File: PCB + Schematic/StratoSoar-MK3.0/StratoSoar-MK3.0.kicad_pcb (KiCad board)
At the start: 2 copper layers, 115 parts, among them J10 SWD, J11 Signal, J12 Rudder, J15 Parachute, J16 Elevator, J18 USB-C, J3 USB-C, J4 J Link, J8 Button, Q1 DMN1019USN-13, Q2 2N3906, Q3 DMN1019USN-13, Q4 DMN1019USN-13, Q5 2N3906, Q6 2N3906, SW1 RESET, SW2 PWR_SW, SW4 RESET, SW5 EEPROM, U1 AMS1117-3.3, U10 ATXK-H11-E-32.768, U11 DSK321STD, U2 ATSAMD21G18A-A, U3 MCP1700x-330xxTT, U4 ATSAMD21G18A-A, U5 BME280, U6 AT24C512C-SSHD-T, U7 ATXK-H11-E-32.768, U8 MAX-M10S, U9 MPU-9250, Y1 32.768 kHz, Y2 32.768kHz

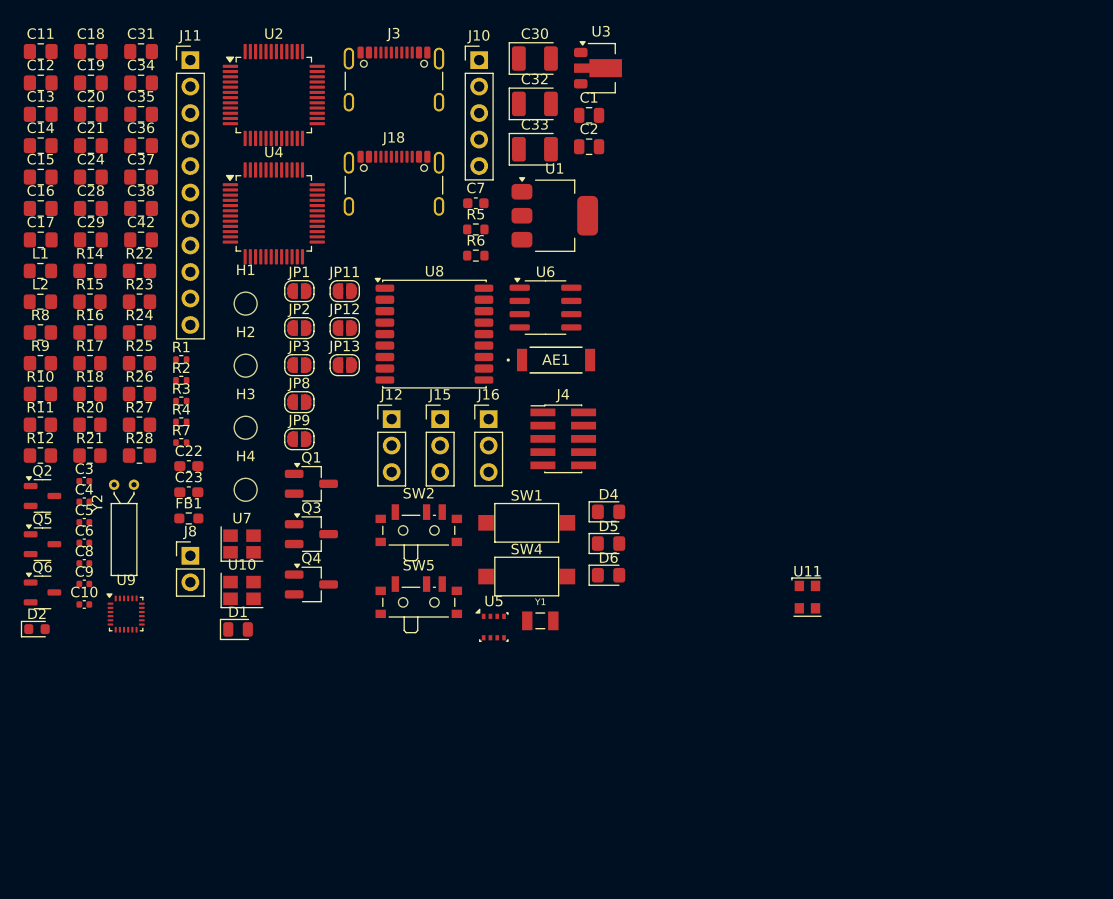
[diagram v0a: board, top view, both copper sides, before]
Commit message: Finished schematic, started PCB
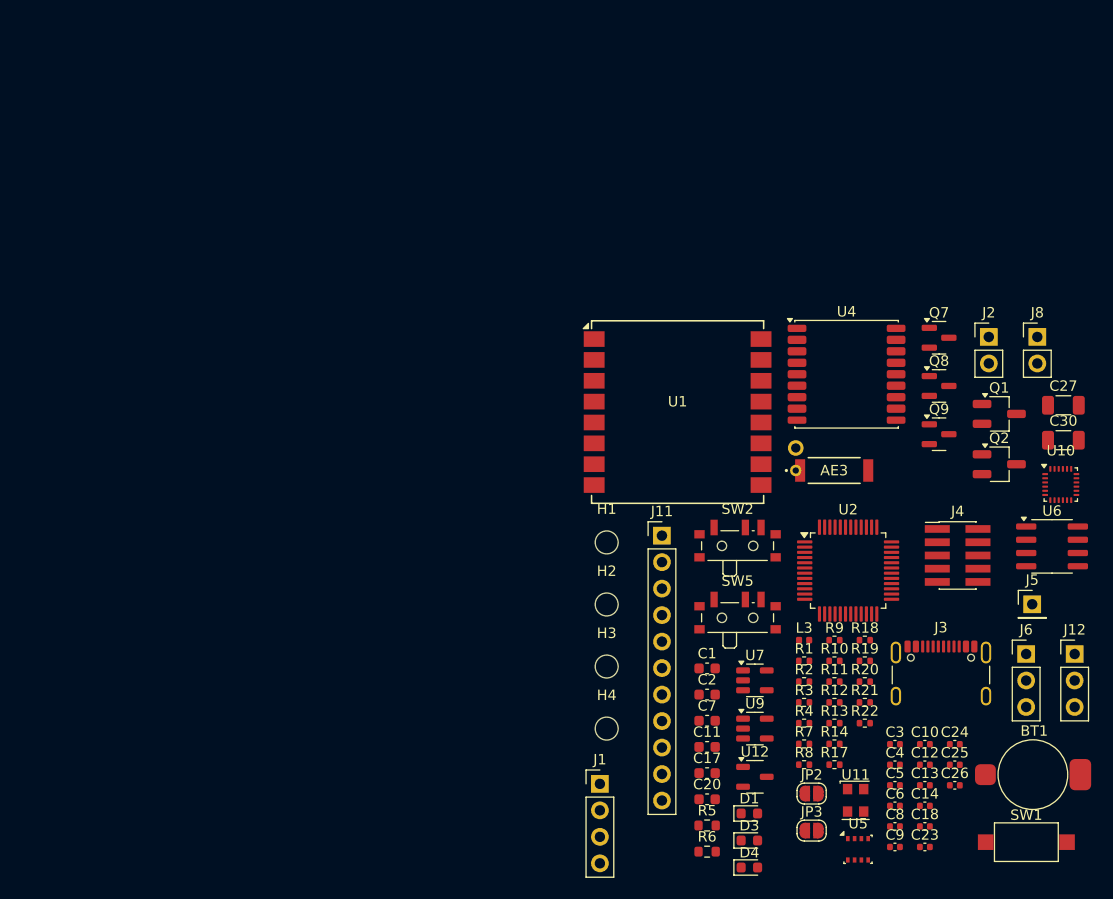
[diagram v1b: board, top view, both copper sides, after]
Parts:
- removed AE1: 1575AT43A0040001E, 1575AT43A0040E:ANT_1575AT_JOT-L
- removed C15, C16, C19, C34, C36, C37, C38, C42: 100nF, Capacitor_SMD:C_0805_2012Metric_Pad1.18x1.45mm_HandSolder
- removed C21: 1 uF, Capacitor_SMD:C_0805_2012Metric_Pad1.18x1.45mm_HandSolder
- removed C22: 100nF, Capacitor_SMD:C_0603_1608Metric_Pad1.08x0.95mm_HandSolder
- removed C28, C29: 22pF, Capacitor_SMD:C_0805_2012Metric_Pad1.18x1.45mm_HandSolder
- removed C31: 100pF, Capacitor_SMD:C_0805_2012Metric_Pad1.18x1.45mm_HandSolder
- removed C32, C33: 47uF, Capacitor_Tantalum_SMD:CP_EIA-3528-21_Kemet-B
- removed C35: 10nF, Capacitor_SMD:C_0805_2012Metric_Pad1.18x1.45mm_HandSolder
- removed D2: LED, LED_SMD:LED_0603_1608Metric
- removed D5: ERR_LED, LED_SMD:LED_0805_2012Metric_Pad1.15x1.40mm_HandSolder
- removed D6: LED, LED_SMD:LED_0805_2012Metric_Pad1.15x1.40mm_HandSolder
- removed FB1: BLM18AG121SN1D, Resistor_SMD:R_0603_1608Metric_Pad0.98x0.95mm_HandSolder
- removed J10: SWD, Connector_PinHeader_2.54mm:PinHeader_1x05_P2.54mm_Vertical
- removed J15: Parachute, Connector_PinHeader_2.54mm:PinHeader_1x03_P2.54mm_Vertical
- removed J16: Elevator, Connector_PinHeader_2.54mm:PinHeader_1x03_P2.54mm_Vertical
- removed J18: USB-C, Connector_USB:USB_C_Receptacle_GCT_USB4105-xx-A_16P_TopMnt_Horizontal
- removed JP1: PWR_EN, Jumper:SolderJumper-2_P1.3mm_Open_RoundedPad1.0x1.5mm
- removed JP11: LED_EN, Jumper:SolderJumper-2_P1.3mm_Open_RoundedPad1.0x1.5mm
- removed JP12: ERR_LED_EN, Jumper:SolderJumper-2_P1.3mm_Open_RoundedPad1.0x1.5mm
- removed JP13: PPS_EN, Jumper:SolderJumper-2_P1.3mm_Open_RoundedPad1.0x1.5mm
- removed JP8, JP9: XO_EN, Jumper:SolderJumper-2_P1.3mm_Open_RoundedPad1.0x1.5mm
- removed L1: 10uH, Inductor_SMD:L_0805_2012Metric_Pad1.15x1.40mm_HandSolder
- removed L2: 33nH, Inductor_SMD:L_0805_2012Metric_Pad1.15x1.40mm_HandSolder
- removed Q3, Q4: DMN1019USN-13, Package_TO_SOT_SMD:SC-59_Handsoldering
- removed Q5, Q6: 2N3906, Package_TO_SOT_SMD:SOT-23-3
- removed R15, R16: 1.8K, Resistor_SMD:R_0805_2012Metric_Pad1.20x1.40mm_HandSolder
- removed R23: 10, Resistor_SMD:R_0805_2012Metric_Pad1.20x1.40mm_HandSolder
- removed R24, R25: 5.1K, Resistor_SMD:R_0805_2012Metric_Pad1.20x1.40mm_HandSolder
- removed R26, R27, R28: 1K, Resistor_SMD:R_0805_2012Metric_Pad1.20x1.40mm_HandSolder
- removed SW4: RESET, Button_Switch_SMD:SW_SPST_CK_RS282G05A3
- removed U3: MCP1700x-330xxTT, Package_TO_SOT_SMD:SOT-89-3
- removed U8: MAX-M10S, RF_GPS:ublox_MAX
- removed Y1: 32.768 kHz, CM7V-T1A-32.768K-12.5PF-20PPM-TA-QA:XTAL_CM7V-T1A-32.768K-12.5PF-20PPM-TA-QA
- removed Y2: 32.768kHz, Crystal:Crystal_C26-LF_D2.1mm_L6.5mm_Horizontal
- added AE3: 1575AT43A0040001E, 1575AT43A0040E:ANT_1575AT_JOT-L, F.Cu at (142.3, 80.7)
- added BT1: MS621R, Battery:MS621R, F.Cu at (156.7, 109.9)
- added C25: 100 pF, Capacitor_SMD:C_0402_1005Metric, F.Cu at (153.8, 108.9)
- added C26: 100 nF, Capacitor_SMD:C_0402_1005Metric, F.Cu at (153.8, 110.9)
- added C27: 47 uF, Capacitor_SMD:C_1206_3216Metric, F.Cu at (164.2, 74.4)
- added D3: YELLOW, LED_SMD:LED_0603_1608Metric, F.Cu at (134.1, 116.2)
- added J1: Power, Connector_PinHeader_2.54mm:PinHeader_1x04_P2.54mm_Vertical, F.Cu at (119.8, 110.7)
- added J2: Battery, Connector_PinHeader_2.54mm:PinHeader_1x02_P2.54mm_Vertical, F.Cu at (157.1, 67.9)
- added J5: Antenna, Connector_PinHeader_2.54mm:PinHeader_1x01_P2.54mm_Vertical, F.Cu at (161.3, 93.5)
- added J6: Rudder, Connector_PinHeader_2.54mm:PinHeader_1x03_P2.54mm_Vertical, F.Cu at (160.7, 98.3)
- added L3: 33 nH, Inductor_SMD:L_0402_1005Metric, F.Cu at (139.4, 97.0)
- added Q7: BSS138, Package_TO_SOT_SMD:SOT-23, F.Cu at (152.3, 68.0)
- added Q8: BSS138, Package_TO_SOT_SMD:SOT-23, F.Cu at (152.3, 72.6)
- added Q9: BSS138, Package_TO_SOT_SMD:SOT-23, F.Cu at (152.3, 77.2)
- added R13: 10 K, Resistor_SMD:R_0402_1005Metric, F.Cu at (142.3, 104.9)
- added R19: 10 K, Resistor_SMD:R_0402_1005Metric, F.Cu at (145.2, 99.0)
- added U12: XC6206P332MR-G, Package_TO_SOT_SMD:SOT-23-3, F.Cu at (134.7, 110.1)
- C1: footprint Capacitor_SMD:C_0805_2012Metric -> Capacitor_SMD:C_0603_1608Metric
- C10, C9: value 22 pF -> 100 nF
- C11: value 10uF -> 1 uF; footprint Capacitor_SMD:C_0805_2012Metric_Pad1.18x1.45mm_HandSolder -> Capacitor_SMD:C_0603_1608Metric
- C12: value 100pF -> 1 uF; footprint Capacitor_SMD:C_0805_2012Metric_Pad1.18x1.45mm_HandSolder -> Capacitor_SMD:C_0402_1005Metric
- C13: value 100nF -> 1 uF; footprint Capacitor_SMD:C_0805_2012Metric_Pad1.18x1.45mm_HandSolder -> Capacitor_SMD:C_0402_1005Metric
- C14: value 100nF -> 100 nF; footprint Capacitor_SMD:C_0805_2012Metric_Pad1.18x1.45mm_HandSolder -> Capacitor_SMD:C_0402_1005Metric
- C17: value 10uF -> 100 nF; footprint Capacitor_SMD:C_0805_2012Metric_Pad1.18x1.45mm_HandSolder -> Capacitor_SMD:C_0603_1608Metric
- C18: value 1uF -> 100 nF; footprint Capacitor_SMD:C_0805_2012Metric_Pad1.18x1.45mm_HandSolder -> Capacitor_SMD:C_0402_1005Metric
- C2: value 10 uF -> 100 nF; footprint Capacitor_SMD:C_0805_2012Metric -> Capacitor_SMD:C_0603_1608Metric
- C20: footprint Capacitor_SMD:C_0805_2012Metric_Pad1.18x1.45mm_HandSolder -> Capacitor_SMD:C_0603_1608Metric
- C23: value 1uF -> 1 uF; footprint Capacitor_SMD:C_0603_1608Metric_Pad1.08x0.95mm_HandSolder -> Capacitor_SMD:C_0402_1005Metric
- C24: footprint Capacitor_SMD:C_0805_2012Metric_Pad1.18x1.45mm_HandSolder -> Capacitor_SMD:C_0402_1005Metric
- C30: value 47uF -> 47 uF; footprint Capacitor_Tantalum_SMD:CP_EIA-3528-21_Kemet-B -> Capacitor_SMD:C_1206_3216Metric
- D1: value PWR_LED -> PWR_RED; footprint LED_SMD:LED_0805_2012Metric -> LED_SMD:LED_0603_1608Metric
- D4: value LED -> YELLOW; footprint LED_SMD:LED_0805_2012Metric_Pad1.15x1.40mm_HandSolder -> LED_SMD:LED_0603_1608Metric
- Q2: value 2N3906 -> DMN1019USN-13; footprint Package_TO_SOT_SMD:SOT-23-3 -> Package_TO_SOT_SMD:SC-59_Handsoldering
- R10: value 220 -> 1 K; footprint Resistor_SMD:R_0805_2012Metric_Pad1.20x1.40mm_HandSolder -> Resistor_SMD:R_0402_1005Metric
- R11, R12, R17, R18, R20: value 10K -> 10 K; footprint Resistor_SMD:R_0805_2012Metric_Pad1.20x1.40mm_HandSolder -> Resistor_SMD:R_0402_1005Metric
- R14, R8, R9: footprint Resistor_SMD:R_0805_2012Metric_Pad1.20x1.40mm_HandSolder -> Resistor_SMD:R_0402_1005Metric
- R21: value 10K -> 10; footprint Resistor_SMD:R_0805_2012Metric_Pad1.20x1.40mm_HandSolder -> Resistor_SMD:R_0402_1005Metric
- R22: value 10 -> 10 K; footprint Resistor_SMD:R_0805_2012Metric_Pad1.20x1.40mm_HandSolder -> Resistor_SMD:R_0402_1005Metric
- U1: value AMS1117-3.3 -> Ra-01; footprint Package_TO_SOT_SMD:SOT-223-3_TabPin2 -> RF_Module:Ai-Thinker-Ra-01-LoRa
- U10: value ATXK-H11-E-32.768 -> ICM-20948; footprint Crystal:Crystal_SMD_Abracon_ABM8AIG-4Pin_3.2x2.5mm -> Sensor_Motion:InvenSense_QFN-24_3x3mm_P0.4mm
- U4: value ATSAMD21G18A-A -> ATGM336H; footprint Package_QFP:TQFP-48_7x7mm_P0.5mm -> RF_GPS:ATGM336H
- U7: value ATXK-H11-E-32.768 -> AT24CS32-STUM; footprint Crystal:Crystal_SMD_Abracon_ABM8AIG-4Pin_3.2x2.5mm -> Package_TO_SOT_SMD:SOT-23-5
- U9: value MPU-9250 -> CJ6206B18M; footprint Sensor_Motion:InvenSense_QFN-24_3x3mm_P0.4mm -> Package_TO_SOT_SMD:SOT-23-5
- moved C18 109.2 mm to (151.0, 114.8)
- moved C12 107.1 mm to (151.0, 108.9)
- moved C13 106.4 mm to (151.0, 110.9)
- moved C14 105.8 mm to (151.0, 112.9)
- moved C24 99.1 mm to (153.8, 106.9)
- moved C11 92.4 mm to (130.1, 107.2)
- moved Q2 91.8 mm to (158.1, 80.1)
- moved C20 88.3 mm to (130.1, 112.2)
- moved R14 84.6 mm to (142.3, 106.9)
- moved R8 84.1 mm to (139.4, 108.9)
- moved J8 83.9 mm to (161.7, 67.9)
- moved R22 82.0 mm to (145.2, 104.9)
- moved C17 81.8 mm to (130.1, 109.7)
- moved C3 81.7 mm to (148.1, 106.9)
- moved C4 81.7 mm to (148.1, 108.9)
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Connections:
- C1 pad 1: +5V -> +3.3V
- C10 pad 1: XOUT -> Net-(U10-REGOUT)
- C11 pad 1: GND -> +3.3V
- C11 pad 2: +3.3V -> GND
- C12 pad 1: Net-(U10-OUTPUT) -> +3.3V
- C12 pad 2: XIN -> GND
- C13 pad 1: +3.3V -> +1V8
- C17 pad 1: Net-(U4-VDDANA) -> GND
- C17 pad 2: GND -> +3.3V
- C18 pad 1: Net-(U4-VDDCORE) -> +3.3V
- C2 pad 1: Net-(JP1-A) -> +3.3V
- C3 pad 1: Net-(JP1-A) -> +1V8
- C30 pad 1: +5V -> VCC
- C4 pad 1: +5V -> USB_IN
- C9 pad 1: XIN -> +1V8
- J11 pad 1: A3 -> unconnected-(J11-Pin_1-Pad1)
- J11 pad 2: A4 -> unconnected-(J11-Pin_2-Pad2)
- J11 pad 3: A5 -> unconnected-(J11-Pin_3-Pad3)
- J11 pad 8: AT_SDA -> unconnected-(J11-Pin_8-Pad8)
- J11 pad 9: AT_SCL -> unconnected-(J11-Pin_9-Pad9)
- J12 pad 2: +5V -> VCC
- J12 pad 3: rOut -> R
- J3 pad A4: +5V -> USB_IN
- J3 pad A9: +5V -> USB_IN
- J3 pad B4: +5V -> USB_IN
- J3 pad B9: +5V -> USB_IN
- J4 pad 10: RST -> RESET
- J8 pad 1: A3 -> unconnected-(J8-Pin_1-Pad1)
- JP3 pad 2: 13 -> LED
- Q2 pad 1: Net-(Q2-B) -> GND
- Q2 pad 2: rOut -> Net-(Q2-G)
- Q2 pad 3: rIn -> Net-(J6-Pin_1)
- R10 pad 1: +3.3V -> Net-(D3-A)
- R10 pad 2: RESET -> PPS
- R11 pad 1: Net-(Q2-B) -> +1V8
- R11 pad 2: rBJT -> SDA_L
- R12 pad 1: GND -> Net-(Q1-G)
- R12 pad 2: Net-(Q1-G) -> GND
- R14 pad 2: rFET -> R_FET
- R17 pad 1: Net-(Q5-B) -> +3.3V
- R17 pad 2: pBJT -> SDA
- R18 pad 1: Net-(Q6-B) -> Net-(Q2-G)
- R18 pad 2: eBJT -> GND
- R20 pad 1: GND -> +1V8
- R20 pad 2: Net-(Q3-G) -> INT_L
- R21 pad 1: GND -> Net-(Q2-G)
- R21 pad 2: Net-(Q4-G) -> L_FET
- R22 pad 1: Net-(Q3-G) -> +3.3V
- R22 pad 2: pFET -> INT
- R4 pad 1: Net-(D2-A) -> Net-(D4-A)
- R7 pad 2: RST -> RESET
- SW1 pad 2: RST -> RESET
- U1 pad 1: GND -> Net-(J5-Pin_1)
- U1 pad 2: Net-(JP1-A) -> GND
- U1 pad 3: +5V -> +3.3V
- U10 pad 1: +3.3V -> unconnected-(U10-RESV_VDDIO-Pad1)
- U10 pad 2: GND -> (no net)
- U10 pad 3: Net-(U10-OUTPUT) -> (no net)
- U10 pad 4: +3.3V -> (no net)
- U11 pad 1: unconnected-(U11-VCC-Pad1) -> +3.3V
- U11 pad 2: unconnected-(U11-GND-Pad2) -> GND
- U11 pad 3: unconnected-(U11-SIG-Pad3) -> Net-(U11-SIG)
- U11 pad 4: unconnected-(U11-VCC-Pad4) -> +3.3V
- U2 pad 2: XOUT -> unconnected-(U2-PA01-Pad2)
- U2 pad 40: RST -> RESET
- U4 pad 1: XIN -> GND
- U4 pad 10: A4 -> GND
- U4 pad 11: rBJT -> GPS
- U4 pad 12: pBJT -> GND
- U4 pad 13: pIn -> (no net)
- U4 pad 14: eIn -> unconnected-(U4-VCC_RF-Pad14)
- U4 pad 15: mcuConnRX -> (no net)
- U4 pad 16: mcuConnTX -> GPS_SDA
- U4 pad 17: +3.3V -> GPS_SCL
- U4 pad 18: GND -> (no net)
- U4 pad 2: XOUT -> TX
- U4 pad 3: ERR_LED -> RX
- U4 pad 4: unconnected-(U4-PA03-Pad4) -> PPS
- U4 pad 5: GND -> +3.3V
- U4 pad 6: Net-(U4-VDDANA) -> V_BAT
- U4 pad 7: BATT -> (no net)
- U4 pad 8: WRITE -> +3.3V
- U4 pad 9: A3 -> GPS_RST
- U7 pad 1: +3.3V -> GPS_SDA
- U7 pad 3: Net-(U7-OUTPUT) -> GPS_SDA
- U9 pad 2: (no net) -> GND
- U9 pad 3: (no net) -> +3.3V
- U9 pad 5: (no net) -> +1V8

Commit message: Basic layout
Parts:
- added C15: 100 nF, Capacitor_SMD:C_0402_1005Metric, F.Cu at (236.7, 87.1)
- C4: footprint Capacitor_SMD:C_0402_1005Metric -> Capacitor_SMD:C_0603_1608Metric
- C7: footprint Capacitor_SMD:C_0603_1608Metric -> Capacitor_SMD:C_0402_1005Metric
- JP2, JP3: moved to B.Cu
- moved U7 164.7 mm to (276.2, 16.6)
- moved C18 161.3 mm to (278.9, 16.5), turned to 90 degrees
- moved D3 158.1 mm to (259.3, 19.6), turned to 90 degrees
- moved C17 156.4 mm to (260.1, 22.9)
- moved BT1 151.1 mm to (278.1, 19.8), turned to -90 degrees
- moved R10 142.8 mm to (260.6, 19.0), turned to 90 degrees
- moved L3 140.0 mm to (261.4, 28.2), turned to 90 degrees
- moved U4 134.7 mm to (267.7, 19.5)
- moved AE3 134.7 mm to (266.5, 28.7)
- moved C8 118.0 mm to (56.0, 41.0), turned to 90 degrees
- moved C5 115.5 mm to (60.7, 35.3)
- moved C3 115.3 mm to (42.0, 152.2)
- moved C9 115.3 mm to (42.0, 162.0)
- moved Q7 115.3 mm to (46.3, 113.2)
- moved Q8 115.3 mm to (46.3, 117.8)
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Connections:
- U7 pad 1: GPS_SDA -> GPS_SCL
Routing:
- net GND: track 0.00 -> 62.2 mm, vias 0 -> 20
- net +3.3V: track 0.00 -> 28.3 mm, vias 0 -> 9
- net VCC: track 0.00 -> 8.99 mm
- net USB_IN: track 0.00 -> 8.58 mm
- net Net-(SW5-B): track 0.00 -> 5.96 mm
- net SCL: track 0.00 -> 5.27 mm
- net Net-(Q1-G): track 0.00 -> 4.99 mm
- net Net-(Q2-G): track 0.00 -> 4.99 mm
- net SDA: track 0.00 -> 3.54 mm
- net Net-(J6-Pin_1): track 0.00 -> 3.39 mm
- net Net-(J12-Pin_1): track 0.00 -> 3.05 mm
- net GPS_SCL: track 0.00 -> 2.87 mm
- net GPS_SDA: track 0.00 -> 2.75 mm
- net BATT: track 0.00 -> 2.46 mm
- net PPS: track 0.00 -> 2.42 mm
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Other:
- copper layers 2 -> 4

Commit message: IMU work
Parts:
- moved AE3 199.5 mm to (75.8, 87.0)
- moved C17 199.5 mm to (69.3, 81.2)
- moved D3 199.5 mm to (68.6, 77.9)
- moved U4 199.5 mm to (76.9, 77.8)
- moved U7 199.5 mm to (85.5, 74.9)
- moved BT1 199.5 mm to (87.4, 78.1)
- moved C18 199.5 mm to (88.1, 74.8)
- moved L3 199.5 mm to (70.6, 86.5)
- moved R10 199.5 mm to (69.8, 77.4)
- moved C2 78.4 mm to (178.9, 40.9), turned to 90 degrees
- moved C1 77.4 mm to (180.5, 40.9), turned to 90 degrees
- moved U1 71.0 mm to (191.5, 44.9)
- moved R7 69.4 mm to (164.0, 171.8), turned to 90 degrees
- moved J5 63.5 mm to (183.5, 34.0)
- moved SW1 55.0 mm to (158.5, 171.3)
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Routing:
- net +3.3V: track 28.3 -> 46.5 mm, vias 9 -> 16
- net GND: track 62.2 -> 79.3 mm, vias 20 -> 27
- net +1V8: track 0.00 -> 9.18 mm
- net Net-(J5-Pin_1): track 0.00 -> 3.91 mm
- net SCL_L: track 0.00 -> 2.05 mm
- net INT_L: track 0.00 -> 2.05 mm
- net SDA_L: track 0.00 -> 2.05 mm
- net SDA: track 3.54 -> 5.18 mm
- net SCL: track 5.27 -> 6.90 mm
- net INT: track 0.00 -> 1.63 mm
- net RESET: track 0.00 -> 1.60 mm
- net Net-(U11-SIG): track 0.00 -> 1.52 mm
- net Net-(U10-REGOUT): track 0.00 -> 1.39 mm

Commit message: Code, licensing
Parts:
- moved C12 33.4 mm to (71.5, 115.8), turned to 180 degrees
- moved U9 30.6 mm to (70.7, 113.2), turned to 90 degrees
- moved C13 28.0 mm to (70.0, 110.6), turned to 0 degrees
- moved Q7 26.0 mm to (68.8, 108.1)
- moved R19 26.0 mm to (68.0, 105.6)
- moved R13 26.0 mm to (68.0, 110.5)
- moved C9 20.8 mm to (68.3, 113.8)
- moved C10 20.8 mm to (66.9, 116.0)
- moved C3 20.8 mm to (65.0, 116.0)
- moved U10 20.8 mm to (65.7, 113.3)
- moved R11 19.6 mm to (64.6, 110.5)
- moved Q8 19.6 mm to (65.3, 108.1)
- moved R17 19.6 mm to (64.6, 105.6)
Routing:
- net +1V8: track 9.18 -> 24.6 mm
- net SCL_L: track 2.05 -> 6.20 mm
- net SDA_L: track 2.05 -> 3.49 mm
- net GND: track 79.3 -> 80.7 mm

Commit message: PCB
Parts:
- removed J11: Signal, Connector_PinHeader_2.54mm:PinHeader_1x11_P2.54mm_Vertical
- added J7: Signal, Connector_PinHeader_2.54mm:PinHeader_1x09_P2.54mm_Vertical, F.Cu at (159.8, 74.7)
- added R15: 1.8 K, Resistor_SMD:R_0603_1608Metric, F.Cu at (85.0, 73.3)
- added R16: 1.8 K, Resistor_SMD:R_0603_1608Metric, F.Cu at (85.0, 78.4)
- BT1: moved to B.Cu
- D1: value PWR_RED -> ERR_RED
- JP2: value PWR_LED_EN -> ERR_LED_EN
- moved C5 124.6 mm to (174.1, 86.7), turned to -90 degrees
- moved C7 123.2 mm to (173.9, 88.8), turned to -90 degrees
- moved C8 119.7 mm to (168.4, 82.0), turned to 0 degrees
- moved C6 116.6 mm to (170.7, 94.2), turned to 180 degrees
- moved U2 115.5 mm to (167.9, 88.3), turned to -90 degrees
- moved R6 110.0 mm to (166.2, 95.5), turned to 180 degrees
- moved R5 109.4 mm to (166.2, 97.0), turned to 180 degrees
- moved J3 105.4 mm to (190.0, 94.1), turned to 90 degrees
- moved C4 100.0 mm to (184.3, 97.3), turned to -90 degrees
- moved R2 98.5 mm to (184.2, 95.3), turned to 180 degrees
- moved R1 96.8 mm to (184.2, 92.3), turned to 180 degrees
- moved J1 79.2 mm to (192.4, 79.1)
- moved U1 69.5 mm to (167.0, 110.0), turned to -90 degrees
- moved J5 69.0 mm to (159.8, 98.8)
- moved H4 66.7 mm to (187.1, 109.6)
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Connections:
- J12 pad 3: R -> RIGHT
- J6 pad 3: L -> LEFT
- J8 pad 1: unconnected-(J8-Pin_1-Pad1) -> GND
- J8 pad 2: GND -> BTN
- JP2 pad 2: +3.3V -> ERR
- U1 pad 5: unconnected-(U1-DIO0-Pad5) -> DIO0
- U2 pad 11: D8 -> L_FET
- U2 pad 12: D9 -> RIGHT
- U2 pad 13: D4 -> BTN
- U2 pad 15: D1 -> TX
- U2 pad 16: D0 -> RX
- U2 pad 24: D5 -> DIO0
- U2 pad 25: D11 -> GPS_EN
- U2 pad 26: D13 -> LED
- U2 pad 27: D10 -> LEFT
- U2 pad 28: D12 -> ERR
- U2 pad 29: D6 -> LORA_RST
- U2 pad 3: A0 -> BATT
- U2 pad 30: D7 -> R_FET
- U4 pad 5: +3.3V -> GPS_EN
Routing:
- net VCC: track 8.99 -> 55.2 mm, vias 0 -> 1
- net +BATT: track 0.00 -> 32.6 mm, vias 0 -> 1
- net +3.3V: track 46.5 -> 73.9 mm, vias 16 -> 15
- net Net-(J5-Pin_1): track 3.91 -> 23.2 mm
- net USB_IN: track 8.58 -> 26.2 mm
- net GND: track 80.7 -> 97.6 mm, vias 27 -> 30
- net V_BAT: track 0.00 -> 8.92 mm, vias 0 -> 1
- net D2: track 0.00 -> 4.77 mm
- net GPS_SDA: track 2.75 -> 4.62 mm
- net GPS_SCL: track 2.87 -> 4.01 mm
- net ERR: track 0.00 -> 0.11 mm, vias 0 -> 1
- added copper zone on In2.Cu, net +3.3V
- added copper zone on In1.Cu, net GND
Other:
- board outline added: 253.4 x 174.4 mm

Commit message: Finished all connections on PCB
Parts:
- removed Q9: BSS138, Package_TO_SOT_SMD:SOT-23
- removed R20, R22: 10 K, Resistor_SMD:R_0402_1005Metric
- moved C12 119.9 mm to (188.1, 87.9)
- moved C13 119.9 mm to (186.6, 82.7)
- moved C9 119.9 mm to (185.0, 85.9)
- moved Q7 119.9 mm to (185.4, 80.2)
- moved Q8 119.9 mm to (182.0, 80.2)
- moved R13 119.9 mm to (184.6, 82.7)
- moved R17 119.9 mm to (181.2, 77.7)
- moved R19 119.9 mm to (184.6, 77.7)
- moved U10 119.9 mm to (182.3, 85.4)
- moved U9 119.9 mm to (187.4, 85.3)
- moved C10 119.9 mm to (183.6, 88.1)
- moved C3 119.9 mm to (181.7, 88.1)
- moved R11 119.9 mm to (181.2, 82.7)
- moved D3 113.9 mm to (182.4, 74.8), turned to -90 degrees
- moved C17 112.8 mm to (181.7, 71.5), turned to 180 degrees
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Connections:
- J7 pad 4: MISO -> D3
- J7 pad 7: D3 -> MISO
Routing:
- net L_FET: track 0.00 -> 59.7 mm, vias 0 -> 2
- net SDA: track 5.18 -> 60.2 mm, vias 0 -> 2
- net SCL: track 6.90 -> 57.6 mm, vias 0 -> 3
- net MOSI: track 0.00 -> 44.4 mm, vias 0 -> 1
- net LEFT: track 0.00 -> 43.7 mm, vias 0 -> 2
- net GPS_EN: track 0.00 -> 42.0 mm, vias 0 -> 4
- net SCK: track 0.00 -> 39.4 mm, vias 0 -> 1
- net RIGHT: track 0.00 -> 39.4 mm, vias 0 -> 1
- net MISO: track 0.00 -> 37.1 mm, vias 0 -> 2
- net CS: track 0.00 -> 34.1 mm, vias 0 -> 2
- net BATT: track 2.46 -> 32.2 mm, vias 0 -> 2
- net R_FET: track 0.00 -> 29.1 mm, vias 0 -> 2
- net RX: track 0.00 -> 27.3 mm
- net TX: track 0.00 -> 25.1 mm, vias 0 -> 2
- net D-: track 2.36 -> 23.8 mm
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
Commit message: Finished PCB, working on silkscreen
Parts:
- J1: renamed from J7; moved to B.Cu
- J2: renamed from J1; moved to B.Cu
- J6: renamed from J5; moved to B.Cu
- J7: renamed from J2; moved to B.Cu
- J8: renamed from J12; moved to B.Cu
- J9: renamed from J6; moved to B.Cu
- moved H2 72.2 mm to (187.5, 66.7)
- moved H1 53.0 mm to (169.2, 66.7)
- moved C10 3.35 mm to (182.5, 83.7), turned to 180 degrees
- moved C11 3.23 mm to (184.7, 85.1), turned to 90 degrees
- moved C13 3.21 mm to (184.7, 87.0), turned to 90 degrees
- moved U7 0.91 mm to (182.0, 86.3), turned to 90 degrees
- turned J1 to 180 degrees
- turned J2 to 180 degrees
- turned J6 to 180 degrees
- turned J7 to 90 degrees
- turned J8 to 90 degrees
- turned J9 to 90 degrees
- renumbered AE3 to AE1, C17 to C1, C9 to C10, C10 to C11, C5 to C12, C3 to C13, C12 to C14, C7 to C15, C6 to C16, C4 to C17, C2 to C18, C1 to C19, C15 to C2, C24 to C21, C11 to C22, C30 to C23, C27 to C24, C18 to C3, C14 to C4, C23 to C5, C25 to C6, C8 to C7, C26 to C8, C13 to C9, D3 to D1, D4 to D2, D1 to D3, J8 to J3, J3 to J4, J4 to J5, JP3 to JP1, L3 to L1, Q8 to Q1, Q7 to Q2, Q1 to Q3, Q2 to Q4, R16 to R1, R4 to R10, R2 to R11, R6 to R12, R5 to R13, R3 to R14, R9 to R15, R8 to R16, R12 to R17, R14 to R19, R10 to R2, R21 to R20, R17 to R3, R19 to R4, R15 to R5, R7 to R6, R11 to R7, R13 to R8, R1 to R9, SW5 to SW1, SW1 to SW2, SW2 to SW3, U6 to U1, U1 to U10, U4 to U2, U7 to U3, U5 to U4, U11 to U5, U9 to U6, U10 to U7, U2 to U8, U12 to U9
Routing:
- net SCL_L: track 6.20 -> 17.7 mm, vias 0 -> 2
- net SDA_L: track 3.49 -> 10.4 mm
- net +1V8: track 22.9 -> 21.5 mm
- net Net-(J5-Pin_1): track 22.9 -> 21.6 mm
- net GND: track 101.3 -> 102.3 mm
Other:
- board size 253.4 x 174.4 mm -> 36.4 x 55.2 mm
- board text added: "+ -"
- board text added: "SWD/JLink"
- board text added: "StratoSoar MK3.0"
